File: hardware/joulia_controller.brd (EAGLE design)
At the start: 32.1 x 61 mm, 29 parts, among them IC1 LM2902D, IC2 LM2902D, U1 MMBT2222ALT1G, U2 MMBT2222ALT1G

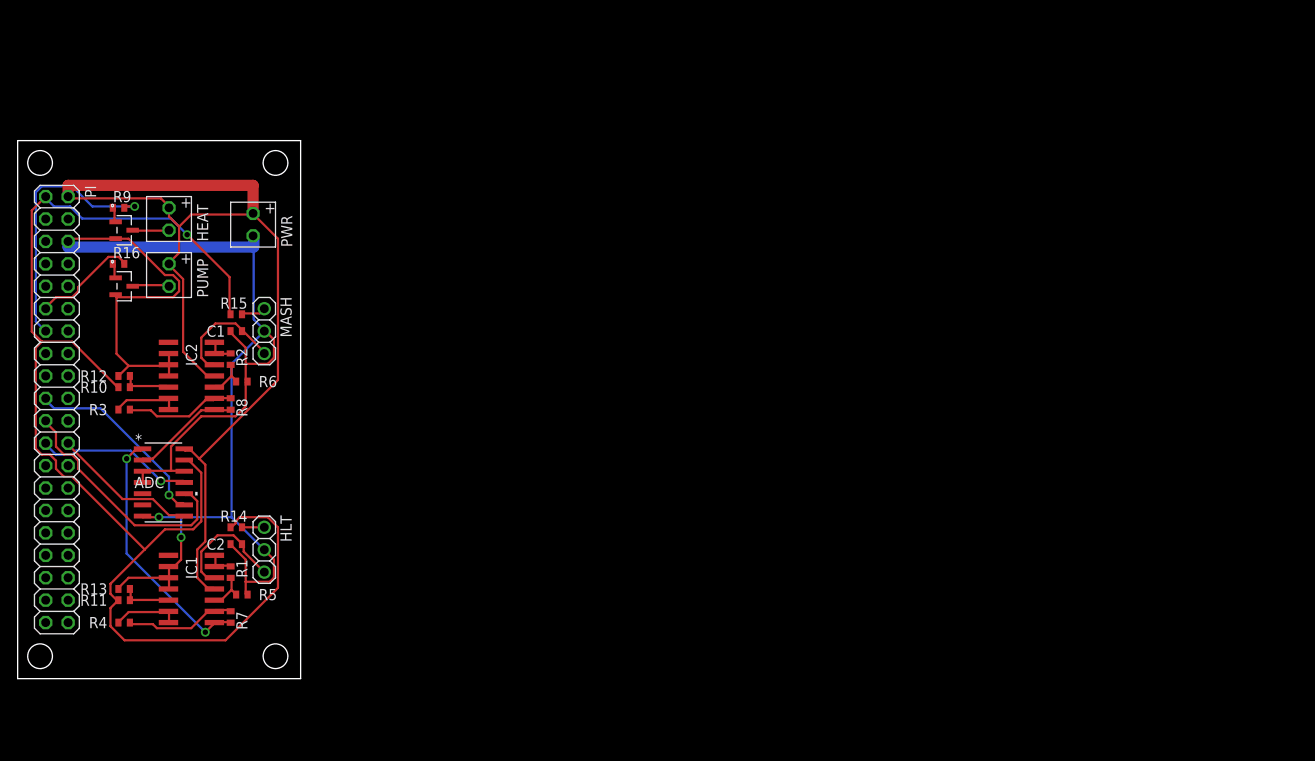
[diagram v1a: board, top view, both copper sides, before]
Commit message: Adding Triac and Heatsink
Need opto-isolation and power terminals.
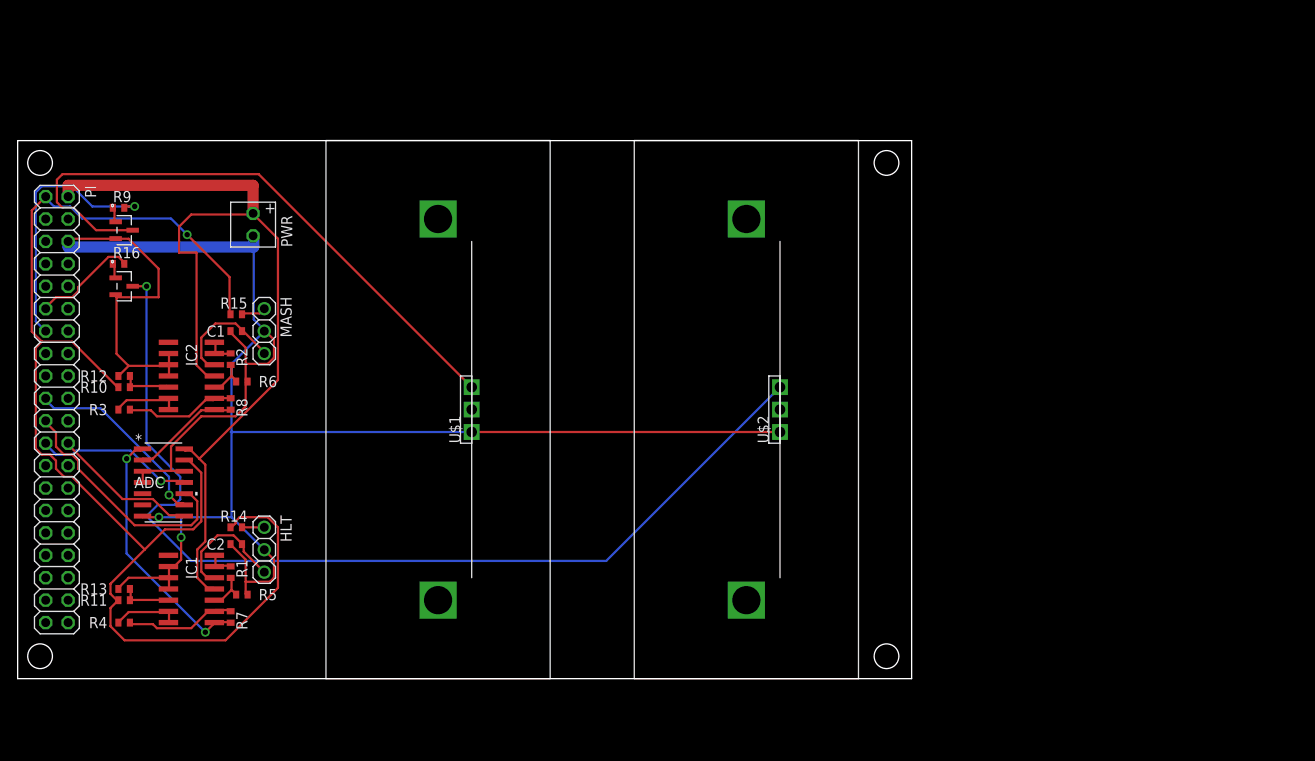
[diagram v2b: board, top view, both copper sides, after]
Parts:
- removed HEAT, PUMP: MTA-100-2HDR2, digikey:HDR2
- added U$1, U$2: T3050H-6I, digikey:TO-220
- added U$3, U$4: VM1-038-1AE, digikey:VM1-038-1AE
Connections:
- net +5V: no longer HEAT.A1, PUMP.A1
- net GND: now also U$1.A1, U$2.A1
- net N$13: now also U$1.G; no longer HEAT.A2
- net N$14: now also U$2.G; no longer PUMP.A2
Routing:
- net N$14: track 4.37 -> 114.0 mm, vias 0 -> 1
- net N$13: track 4.22 -> 69.7 mm
- net GND: track 178.1 -> 236.9 mm
- net +5V: track 120.6 -> 106.3 mm
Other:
- board size 32.1 x 61 mm -> 101.3 x 61 mm
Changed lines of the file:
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@@
 <board>
 <plain>
-<wire x1="0" y1="0" x2="32.055" y2="0" width="0" layer="20"/>
-<wire x1="32.055" y1="0" x2="32.055" y2="60.95" width="0" layer="20"/>
-<wire x1="32.055" y1="60.95" x2="0" y2="60.95" width="0" layer="20"/>
+<wire x1="0" y1="0" x2="101.27" y2="0" width="0" layer="20"/>
+<wire x1="101.27" y1="0" x2="101.27" y2="60.95" width="0" layer="20"/>
+<wire x1="101.27" y1="60.95" x2="0" y2="60.95" width="0" layer="20"/>
 <wire x1="0" y1="60.95" x2="0" y2="0" width="0" layer="20"/>
 <hole x="2.54" y="58.42" drill="2.8"/>
-<hole x="29.21" y="58.42" drill="2.8"/>
+<hole x="98.425" y="58.42" drill="2.8"/>
 <hole x="2.54" y="2.54" drill="2.8"/>
-<hole x="29.21" y="2.54" drill="2.8"/>
+<hole x="98.425" y="2.54" drill="2.8"/>
 <text x="28.575" y="5.715" size="1.778" layer="26" rot="MR90">JOULIA HOMEBREW CONTROLLER</text>
 <text x="19.05" y="5.715" size="1.778" layer="26" rot="MR90">WILLIAM SCHMITT
@@
 <attribute name="NAME" x="10.16" y="9.525" size="1.27" layer="25" rot="R180"/>
 </element>
-<element name="HEAT" library="digikey" package="HDR2" value="MTA-100-2HDR2" x="17.145" y="52.07"/>
-<element name="PUMP" library="digikey" package="HDR2" value="MTA-100-2HDR2" x="17.145" y="45.72"/>
 <element name="U1" library="digikey" package="SOT-23" value="MMBT2222ALT1G" x="12.065" y="50.8" smashed="yes" rot="R270">
 <attribute name="MANUFACTURER_PART_NUMBER" value="MMBT2222ALT1G" x="12.065" y="50.8" size="1.778" layer="27" rot="R270" display="off"/>
@@
 <attribute name="NAME" x="10.795" y="47.625" size="1.27" layer="25"/>
 </element>
+<element name="U$1" library="digikey" package="TO-220" value="T3050H-6I" x="51.435" y="30.48" rot="R90"/>
+<element name="U$2" library="digikey" package="TO-220" value="T3050H-6I" x="86.36" y="30.48" rot="R90"/>
+<element name="U$3" library="digikey" package="VM1-038-1AE" value="VM1-038-1AE" x="47.625" y="30.48" rot="R270"/>
+<element name="U$4" library="digikey" package="VM1-038-1AE" value="VM1-038-1AE" x="82.55" y="30.48" rot="R270"/>
 </elements>
 <signals>
@@
 <wire x1="17.145" y1="35.6616" x2="17.085" y2="35.56" width="0.254" layer="1"/>
 <wire x1="12.573" y1="49.8348" x2="11.2014" y2="49.8348" width="0.254" layer="1"/>
-<wire x1="16.6878" y1="45.72" x2="12.573" y2="49.8348" width="0.254" layer="1"/>
-<wire x1="17.6022" y1="45.72" x2="16.6878" y2="45.72" width="0.254" layer="1"/>
-<wire x1="18.288" y1="45.0342" x2="17.6022" y2="45.72" width="0.254" layer="1"/>
-<wire x1="18.288" y1="43.8912" x2="18.288" y2="45.0342" width="0.254" layer="1"/>
-<wire x1="17.6022" y1="43.2054" x2="18.288" y2="43.8912" width="0.254" layer="1"/>
-<wire x1="11.2014" y1="43.2054" x2="17.6022" y2="43.2054" width="0.254" layer="1"/>
+<wire x1="15.9639" y1="46.4439" x2="16.6878" y2="45.72" width="0" layer="19" extent="1-16"/>
+<wire x1="15.9639" y1="46.4439" x2="12.573" y2="49.8348" width="0.254" layer="1"/>
+<wire x1="11.2014" y1="43.2054" x2="15.9639" y2="43.2054" width="0.254" layer="1"/>
+<wire x1="15.9639" y1="43.2054" x2="17.6022" y2="43.2054" width="0" layer="19" extent="1-16"/>
 <wire x1="11.2014" y1="49.8348" x2="11.0998" y2="49.8475" width="0.254" layer="1"/>
 <wire x1="12.573" y1="11.43" x2="11.43" y2="10.287" width="0.254" layer="1"/>
@@
 <wire x1="25.8318" y1="33.6042" x2="25.8318" y2="30.861" width="0.254" layer="1"/>
 <wire x1="25.8318" y1="33.6042" x2="26.05" y2="33.655" width="0.254" layer="1"/>
-<wire x1="24.2316" y1="35.6616" x2="24.2316" y2="18.288" width="0.254" layer="16"/>
+<wire x1="24.2316" y1="35.6616" x2="24.2316" y2="27.94" width="0.254" layer="16"/>
+<wire x1="24.2316" y1="27.94" x2="24.2316" y2="18.288" width="0.254" layer="16"/>
 <wire x1="27.94" y1="39.37" x2="24.2316" y2="35.6616" width="0.254" layer="16"/>
 <wire x1="5.715" y1="49.53" x2="5.715" y2="49.3776" width="0.254" layer="16"/>
@@
 <wire x1="26.7462" y1="48.895" x2="5.715" y2="48.895" width="1.27" layer="16"/>
 <wire x1="5.715" y1="48.895" x2="5.715" y2="49.53" width="1.27" layer="16"/>
+<contactref element="U$1" pad="A1"/>
+<contactref element="U$2" pad="A1"/>
+<wire x1="24.2316" y1="27.94" x2="51.435" y2="27.94" width="0.254" layer="16"/>
+<wire x1="24.13" y1="27.94" x2="24.2316" y2="27.94" width="0.254" layer="16"/>
+<wire x1="51.435" y1="27.94" x2="86.36" y2="27.94" width="0.254" layer="1"/>
+<wire x1="15.9639" y1="43.2054" x2="15.9639" y2="46.4439" width="0.254" layer="1"/>
 </signal>
 <signal name="N$4">
@@
 <contactref element="PI" pad="2"/>
 <contactref element="ADC" pad="14"/>
-<contactref element="HEAT" pad="A1"/>
 <contactref element="IC1" pad="4"/>
 <contactref element="IC2" pad="4"/>
-<contactref element="PUMP" pad="A1"/>
 <contactref element="PWR" pad="A1"/>
 <wire x1="19.6596" y1="25.8318" x2="18.9738" y2="25.8318" width="0.254" layer="1"/>
@@
 <wire x1="22.1742" y1="10.287" x2="22.285" y2="10.16" width="0.254" layer="1"/>
 <wire x1="21.4884" y1="34.29" x2="22.285" y2="34.29" width="0.254" layer="1"/>
-<wire x1="18.7452" y1="37.0332" x2="21.4884" y2="34.29" width="0.254" layer="1"/>
-<wire x1="18.7452" y1="45.2628" x2="18.7452" y2="37.0332" width="0.254" layer="1"/>
-<wire x1="17.145" y1="46.863" x2="18.7452" y2="45.2628" width="0.254" layer="1"/>
-<wire x1="17.145" y1="46.863" x2="17.145" y2="46.99" width="0.254" layer="1"/>
-<wire x1="17.145" y1="52.3494" x2="17.145" y2="53.34" width="0.254" layer="1"/>
-<wire x1="18.288" y1="51.2064" x2="17.145" y2="52.3494" width="0.254" layer="1"/>
-<wire x1="18.288" y1="48.2346" x2="18.288" y2="51.2064" width="0.254" layer="1"/>
-<wire x1="17.145" y1="47.0916" x2="18.288" y2="48.2346" width="0.254" layer="1"/>
-<wire x1="17.145" y1="47.0916" x2="17.145" y2="46.99" width="0.254" layer="1"/>
+<wire x1="20.2692" y1="35.5092" x2="18.7452" y2="37.0332" width="0" layer="19" extent="1-16"/>
+<wire x1="20.2692" y1="35.5092" x2="21.4884" y2="34.29" width="0.254" layer="1"/>
+<wire x1="18.288" y1="48.2346" x2="18.288" y2="48.26" width="0.254" layer="1"/>
+<wire x1="18.288" y1="48.26" x2="18.288" y2="51.2064" width="0.254" layer="1"/>
 <wire x1="19.6596" y1="52.578" x2="26.5176" y2="52.578" width="0.254" layer="1"/>
 <wire x1="18.288" y1="51.2064" x2="19.6596" y2="52.578" width="0.254" layer="1"/>
 <wire x1="26.5176" y1="52.578" x2="26.67" y2="52.705" width="0.254" layer="1"/>
-<wire x1="16.2306" y1="54.4068" x2="5.715" y2="54.4068" width="0.254" layer="1"/>
-<wire x1="17.145" y1="53.4924" x2="16.2306" y2="54.4068" width="0.254" layer="1"/>
 <wire x1="5.715" y1="54.61" x2="5.715" y2="54.4068" width="0.254" layer="1"/>
-<wire x1="17.145" y1="53.4924" x2="17.145" y2="53.34" width="0.254" layer="1"/>
 <wire x1="29.4894" y1="33.8328" x2="20.574" y2="24.9174" width="0.254" layer="1"/>
 <wire x1="29.4894" y1="49.8348" x2="29.4894" y2="33.8328" width="0.254" layer="1"/>
@@
 <wire x1="26.67" y1="55.88" x2="5.715" y2="55.88" width="1.27" layer="1"/>
 <wire x1="5.715" y1="55.88" x2="5.715" y2="54.61" width="1.27" layer="1"/>
+<wire x1="18.288" y1="48.26" x2="20.2692" y2="48.26" width="0.254" layer="1"/>
+<wire x1="20.2692" y1="48.26" x2="20.2692" y2="35.5092" width="0.254" layer="1"/>
 </signal>
 <signal name="+3V3">
@@
 <signal name="N$13">
 <contactref element="U1" pad="3"/>
-<contactref element="HEAT" pad="A2"/>
-<wire x1="17.145" y1="50.7492" x2="13.0302" y2="50.7492" width="0.254" layer="1"/>
 <wire x1="13.0302" y1="50.7492" x2="13.0302" y2="50.8" width="0.254" layer="1"/>
-<wire x1="17.145" y1="50.7492" x2="17.145" y2="50.8" width="0.254" layer="1"/>
+<contactref element="U$1" pad="G"/>
+<wire x1="8.89" y1="50.8" x2="13.0302" y2="50.8" width="0.254" layer="1"/>
+<wire x1="6.35" y1="53.34" x2="8.89" y2="50.8" width="0.254" layer="1"/>
+<wire x1="5.08" y1="53.34" x2="6.35" y2="53.34" width="0.254" layer="1"/>
+<wire x1="4.445" y1="53.975" x2="5.08" y2="53.34" width="0.254" layer="1"/>
+<wire x1="4.445" y1="56.515" x2="4.445" y2="53.975" width="0.254" layer="1"/>
+<wire x1="5.08" y1="57.15" x2="4.445" y2="56.515" width="0.254" layer="1"/>
+<wire x1="27.305" y1="57.15" x2="5.08" y2="57.15" width="0.254" layer="1"/>
+<wire x1="51.435" y1="33.02" x2="27.305" y2="57.15" width="0.254" layer="1"/>
 </signal>
 <signal name="N$14">
 <contactref element="U2" pad="3"/>
-<contactref element="PUMP" pad="A2"/>
-<wire x1="17.145" y1="44.577" x2="13.0302" y2="44.577" width="0.254" layer="1"/>
 <wire x1="13.0302" y1="44.577" x2="13.0302" y2="44.45" width="0.254" layer="1"/>
-<wire x1="17.145" y1="44.577" x2="17.145" y2="44.45" width="0.254" layer="1"/>
+<contactref element="U$2" pad="G"/>
+<wire x1="14.605" y1="44.45" x2="13.0302" y2="44.45" width="0.254" layer="1"/>
+<wire x1="14.605" y1="26.67" x2="14.605" y2="44.45" width="0.254" layer="16"/>
+<wire x1="18.415" y1="22.86" x2="14.605" y2="26.67" width="0.254" layer="16"/>
+<wire x1="18.415" y1="20.32" x2="18.415" y2="22.86" width="0.254" layer="16"/>
+<wire x1="17.78" y1="19.685" x2="18.415" y2="20.32" width="0.254" layer="16"/>
+<wire x1="15.875" y1="19.685" x2="17.78" y2="19.685" width="0.254" layer="16"/>
+<wire x1="14.605" y1="18.415" x2="15.875" y2="19.685" width="0.254" layer="16"/>
+<wire x1="19.685" y1="13.335" x2="14.605" y2="18.415" width="0.254" layer="16"/>
+<wire x1="66.675" y1="13.335" x2="19.685" y2="13.335" width="0.254" layer="16"/>
+<wire x1="86.36" y1="33.02" x2="66.675" y2="13.335" width="0.254" layer="16"/>
+<via x="14.605" y="44.45" extent="1-16" drill="0.6096"/>
 </signal>
 <signal name="HEOUT">

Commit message: Adding connectors and SSR to board
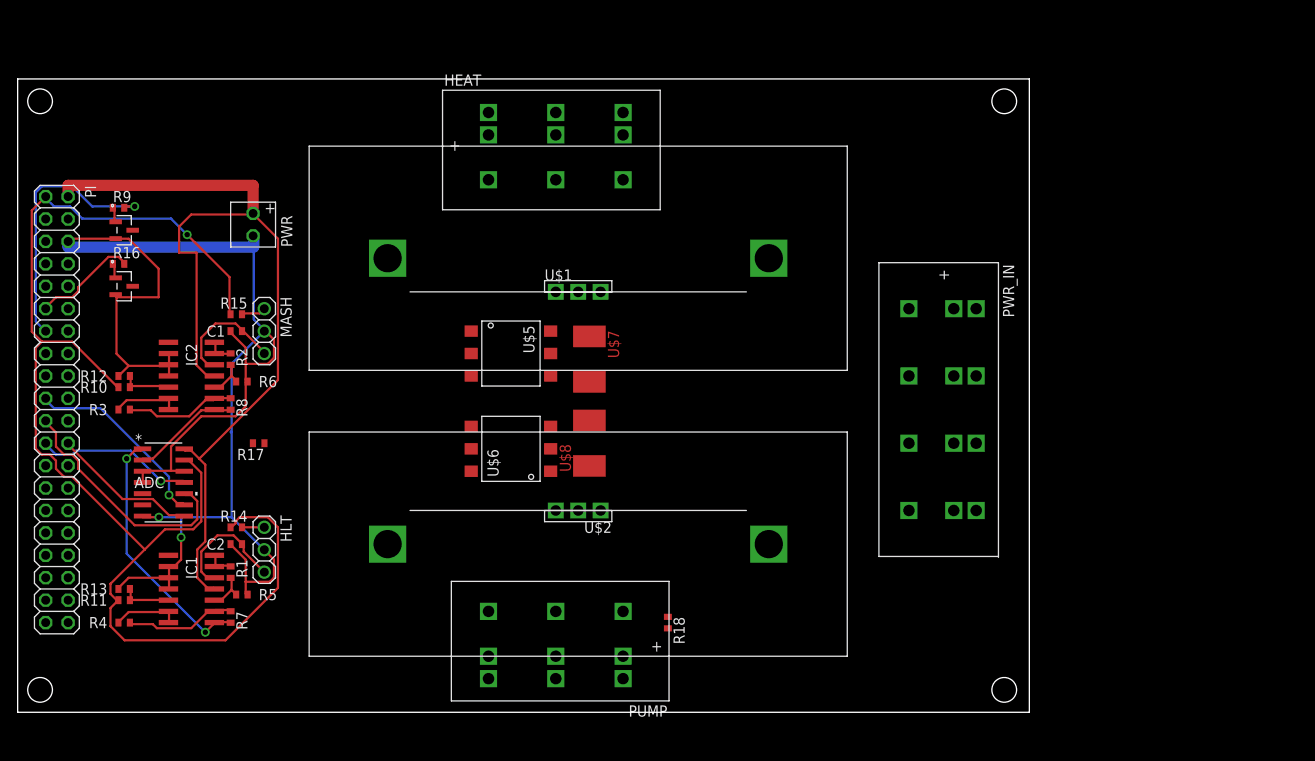
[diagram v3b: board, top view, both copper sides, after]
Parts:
- added HEAT, PUMP: PC1720589, digikey:PC-PCV5/3-G-7.62
- added PWR_IN: PC1720592, digikey:PC-PCV5/4-G-7.62
- added R17, R18: 220, resistor:R0402
- added U$5, U$6: MOC3020S, digikey:6-SMD
- added U$7, U$8: CRM2512, digikey:2512(6432METRIC)
- moved U$2 25.6 mm to (63.5, 19.1), turned to 180 degrees
- moved U$4 24.4 mm to (63.5, 15.2), turned to 0 degrees
- moved U$3 23.4 mm to (63.5, 47.6), turned to 180 degrees
- moved U$1 18.0 mm to (63.5, 43.8), turned to 0 degrees
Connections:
- new net N$17: R18.2, U2.3
- new net N$18: R18.1, U$6.P$5
- new net N$19: U$1.G, U$5.P$3
- new net N$20: U$5.P$1, U$7.P$1
- new net N$21: U$6.P$1, U$8.P$1
- new net N$22: HEAT.P$7, HEAT.P$8, HEAT.P$9, U$1.A2, U$7.P$2
- new net N$23: U$2.G, U$6.P$3
- new net N$24: U$2.A2, U$8.P$2
- new net N$25: HEAT.P$4, HEAT.P$5, HEAT.P$6, PWR_IN.P$7, PWR_IN.P$8, PWR_IN.P$9
- new net N$26: PWR_IN.P$4, PWR_IN.P$5, PWR_IN.P$6, U$1.A1, U$2.A1
- new net N$27: PUMP.P$7, PUMP.P$8, PUMP.P$9, PWR_IN.P$1, PWR_IN.P$2, PWR_IN.P$3
- net +5V: now also U$5.P$6, U$6.P$6
- net GND: now also HEAT.P$1, HEAT.P$2, HEAT.P$3, PUMP.P$1, PUMP.P$2, PUMP.P$3, PWR_IN.P$10, PWR_IN.P$11, PWR_IN.P$12; no longer U$1.A1, U$2.A1
- net N$13: now also R17.2; no longer U$1.G
- net N$14: now also R17.1, U$5.P$5; no longer U$2.G, U2.3
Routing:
- net N$14: track 114.0 -> 0.00 mm, vias 1 -> 0
- net N$13: track 69.7 -> 0.00 mm
- net GND: track 236.9 -> 174.4 mm
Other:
- board size 101.3 x 61 mm -> 114.6 x 71.7 mm

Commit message: Routing and rearrangement for power
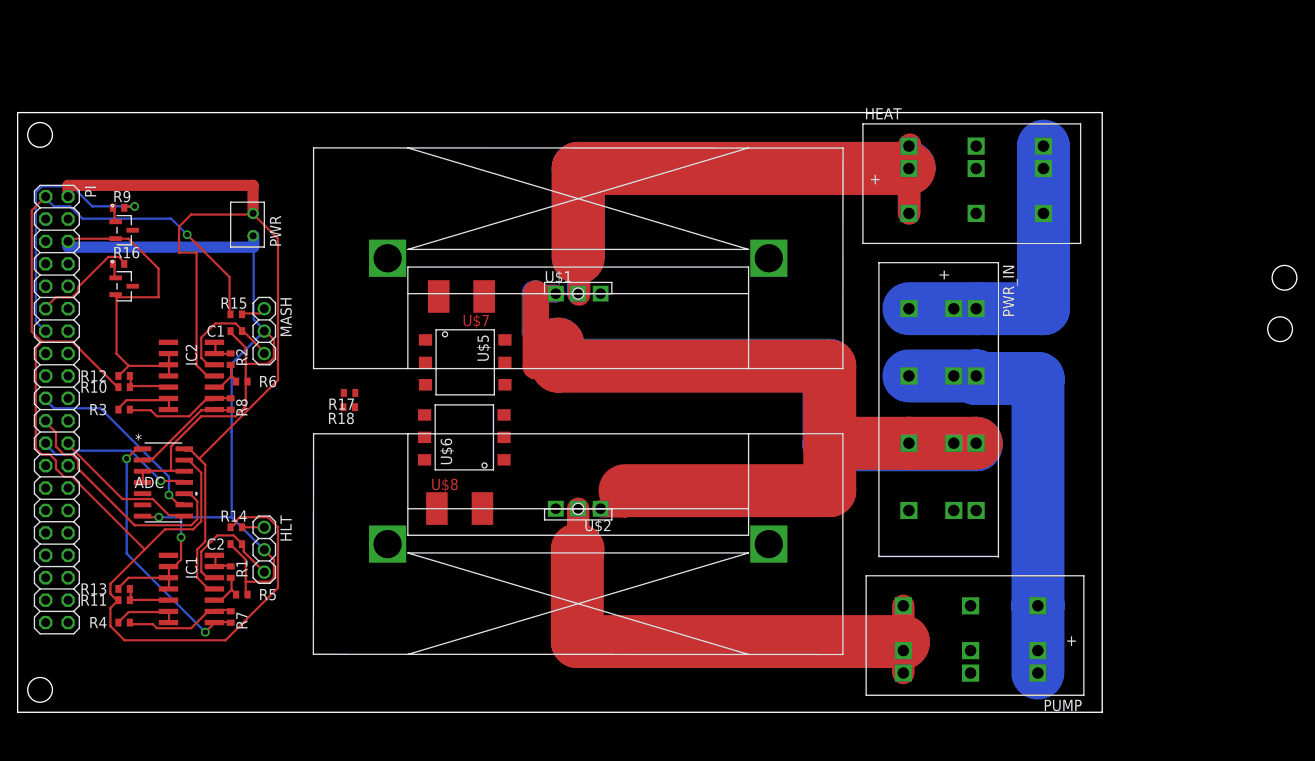
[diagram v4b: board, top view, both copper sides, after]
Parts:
- moved HEAT 47.8 mm to (108.6, 60.3)
- moved PUMP 47.0 mm to (108.0, 0.64)
- moved R18 43.6 mm to (37.6, 30.8), turned to 180 degrees
- moved U$8 16.5 mm to (50.1, 19.3), turned to 0 degrees
- moved U$7 16.1 mm to (50.3, 43.3), turned to 180 degrees
- moved R17 11.8 mm to (37.6, 32.4)
- moved U$6 5.44 mm to (50.6, 27.3)
- moved U$5 5.27 mm to (50.7, 35.8)
- moved U$2 0.20 mm to (63.5, 19.2)
- moved U$1 0.20 mm to (63.5, 43.6)
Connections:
- net N$24: now also PUMP.P$4, PUMP.P$5, PUMP.P$6
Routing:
- net N$26: track 0.00 -> 177.6 mm
- net N$24: track 0.00 -> 63.7 mm
- net N$27: track 0.00 -> 48.6 mm
- net N$28: track 0.00 -> 47.6 mm
- net N$30: track 0.00 -> 47.6 mm
- net N$25: track 0.00 -> 41.1 mm
- net N$22: track 0.00 -> 11.6 mm
- net N$31: track 0.00 -> 7.84 mm
- net N$29: track 0.00 -> 3.80 mm
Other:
- board size 114.6 x 71.7 mm -> 122.9 x 67.9 mm
